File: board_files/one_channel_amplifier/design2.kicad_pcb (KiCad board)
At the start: 2 copper layers, 50.8 x 50.8 mm, 27 parts, among them J1 Screw_Terminal_01x02, J2 Screw_Terminal_01x02, J3 Screw_Terminal_01x02, J4 Conn_01x02, J5 Conn_01x02, J6 Screw_Terminal_01x02, U1 LM3886

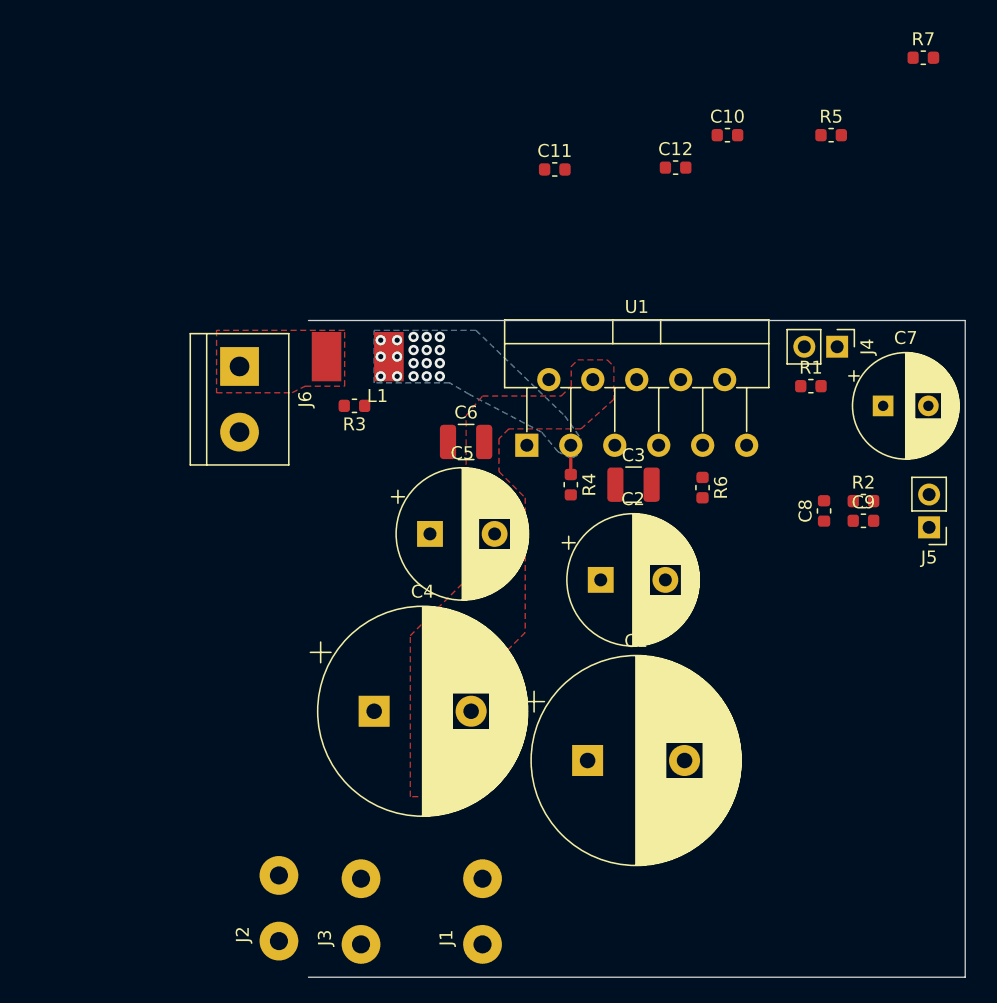
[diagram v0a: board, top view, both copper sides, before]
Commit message: completed component placement
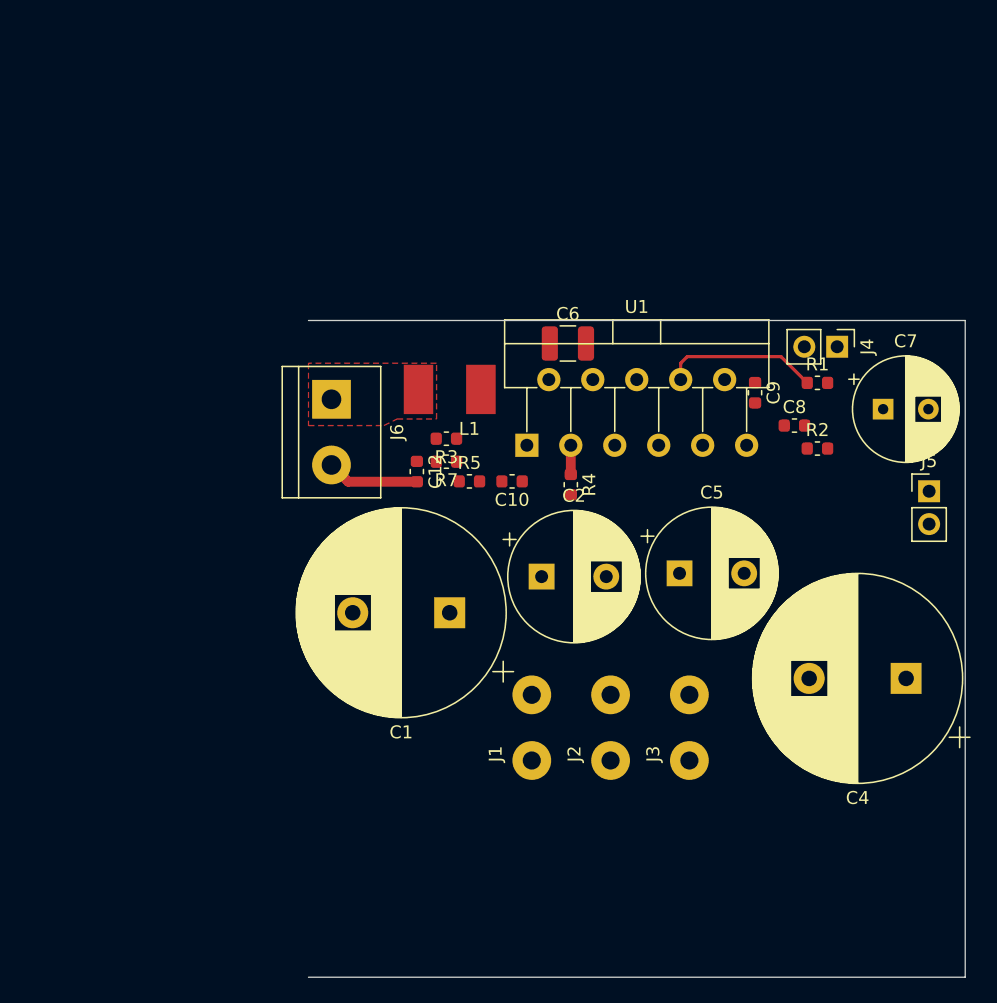
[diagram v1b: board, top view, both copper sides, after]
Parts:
- removed C11: 0.1uF, Capacitor_SMD:C_0603_1608Metric
- removed C3: 4.7uF, Resistor_SMD:R_1210_3225Metric
- removed R6: 6.34k, Resistor_SMD:R_0603_1608Metric
- moved R7 48.3 mm to (137.7, 87.1), turned to 180 degrees
- moved C4 41.2 mm to (173.2, 103.9), turned to 180 degrees
- moved R5 38.7 mm to (139.4, 88.6)
- moved C10 31.5 mm to (142.7, 88.6), turned to 180 degrees
- moved C12 30.9 mm to (135.4, 87.9), turned to 270 degrees
- moved J2 29.2 mm to (150.4, 110.2)
- moved J3 29.1 mm to (156.5, 110.2)
- moved C5 19.5 mm to (155.7, 95.8)
- moved C1 15.6 mm to (137.9, 98.8), turned to 180 degrees
- moved J1 14.7 mm to (144.3, 110.2)
- moved C9 13.0 mm to (161.5, 81.8), turned to 270 degrees
- moved C6 11.0 mm to (147.1, 78.0)
- moved J6 7.55 mm to (128.8, 82.3)
- moved L1 7.55 mm to (137.9, 81.5)
- moved R3 7.55 mm to (137.7, 85.3)
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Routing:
- net Net-(C7-Pad1): track 0.00 -> 12.1 mm
- net GND: track 0.00 -> 7.14 mm
- net Net-(L1-Pad1): vias 18 -> 0
- removed copper zone on B.Cu, net Net-(L1-Pad1)
- removed copper zone on F.Cu, net VEE

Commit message: added 3rd design iteration
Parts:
- added C11: 0.1uF, Capacitor_SMD:C_0603_1608Metric, F.Cu at (156.7, 88.6)
- added C3: 4.7uF, Resistor_SMD:R_1210_3225Metric, F.Cu at (152.1, 88.9)
- added R6: 6.34k, Resistor_SMD:R_0603_1608Metric, F.Cu at (158.5, 88.6)
- moved J1 35.3 mm to (109.0, 108.7)
- moved J2 35.3 mm to (115.1, 108.7)
- moved J3 35.3 mm to (121.2, 108.7)
- moved C1 14.2 mm to (147.3, 109.5)
- moved C4 10.9 mm to (164.1, 109.7)
- moved R3 2.81 mm to (137.9, 82.5)
- moved J6 2.54 mm to (128.8, 79.8)
- moved L1 2.54 mm to (137.9, 79.0)
- moved C12 0.92 mm to (134.9, 87.1), turned to 180 degrees
- moved R5 0.36 mm to (139.7, 88.9)
- moved C10 0.25 mm to (142.7, 88.9)
- moved R2 0.25 mm to (166.1, 86.1)
- moved R7 0.25 mm to (137.9, 87.1)
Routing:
- net GND: track 7.14 -> 38.0 mm, vias 0 -> 2
- net Net-(J5-Pad2): track 0.00 -> 10.5 mm
- net Net-(C8-Pad2): track 0.00 -> 9.46 mm
- net Net-(C10-Pad1): track 0.00 -> 9.37 mm
- net Net-(L1-Pad1): track 2.26 -> 8.69 mm, vias 0 -> 16
- net Net-(C11-Pad1): track 0.00 -> 1.78 mm
- net Net-(C12-Pad1): track 0.00 -> 1.47 mm
- net Net-(C10-Pad2): track 0.00 -> 1.47 mm
- net Net-(J6-Pad1): vias 0 -> 18
- added copper zone on B.Cu, net Net-(J6-Pad1)
- added copper zone on B.Cu, net Net-(L1-Pad1)
- added copper zone on F.Cu, net Net-(L1-Pad1)
